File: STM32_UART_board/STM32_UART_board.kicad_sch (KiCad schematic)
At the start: 32 parts, among them J1 SWD, J2 Scooter, J3 Conn_01x10, Q1 AO4612_C4748739, SW1 SW_Push, SW2 SW_Push, U1 BAS70-05, U2 LM2574HVM-5, U3 AZ1117-3.3, U4 STM32C011F6Px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

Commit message: added testpoints to the remaining pins
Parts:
- added JP1, JP2, JP3: SolderJumper_3_Open, Jumper:SolderJumper-3_P1.3mm_Open_Pad1.0x1.5mm, symbol Jumper:SolderJumper_3_Open
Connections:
- net BOOT0_USART1_RX: now also JP2.3 (B)
- net BOOT0_USART1_TX: now also JP2.2 (C)
- net PA0: now also JP1.1 (A)
- net PA2: now also JP1.2 (C)
- net PA3: now also JP1.3 (B)
- net PA4: now also JP2.1 (A)
- net PB6: now also JP3.1 (A)
- net PB7: now also JP3.2 (C)
- net PC15: now also JP3.3 (B)

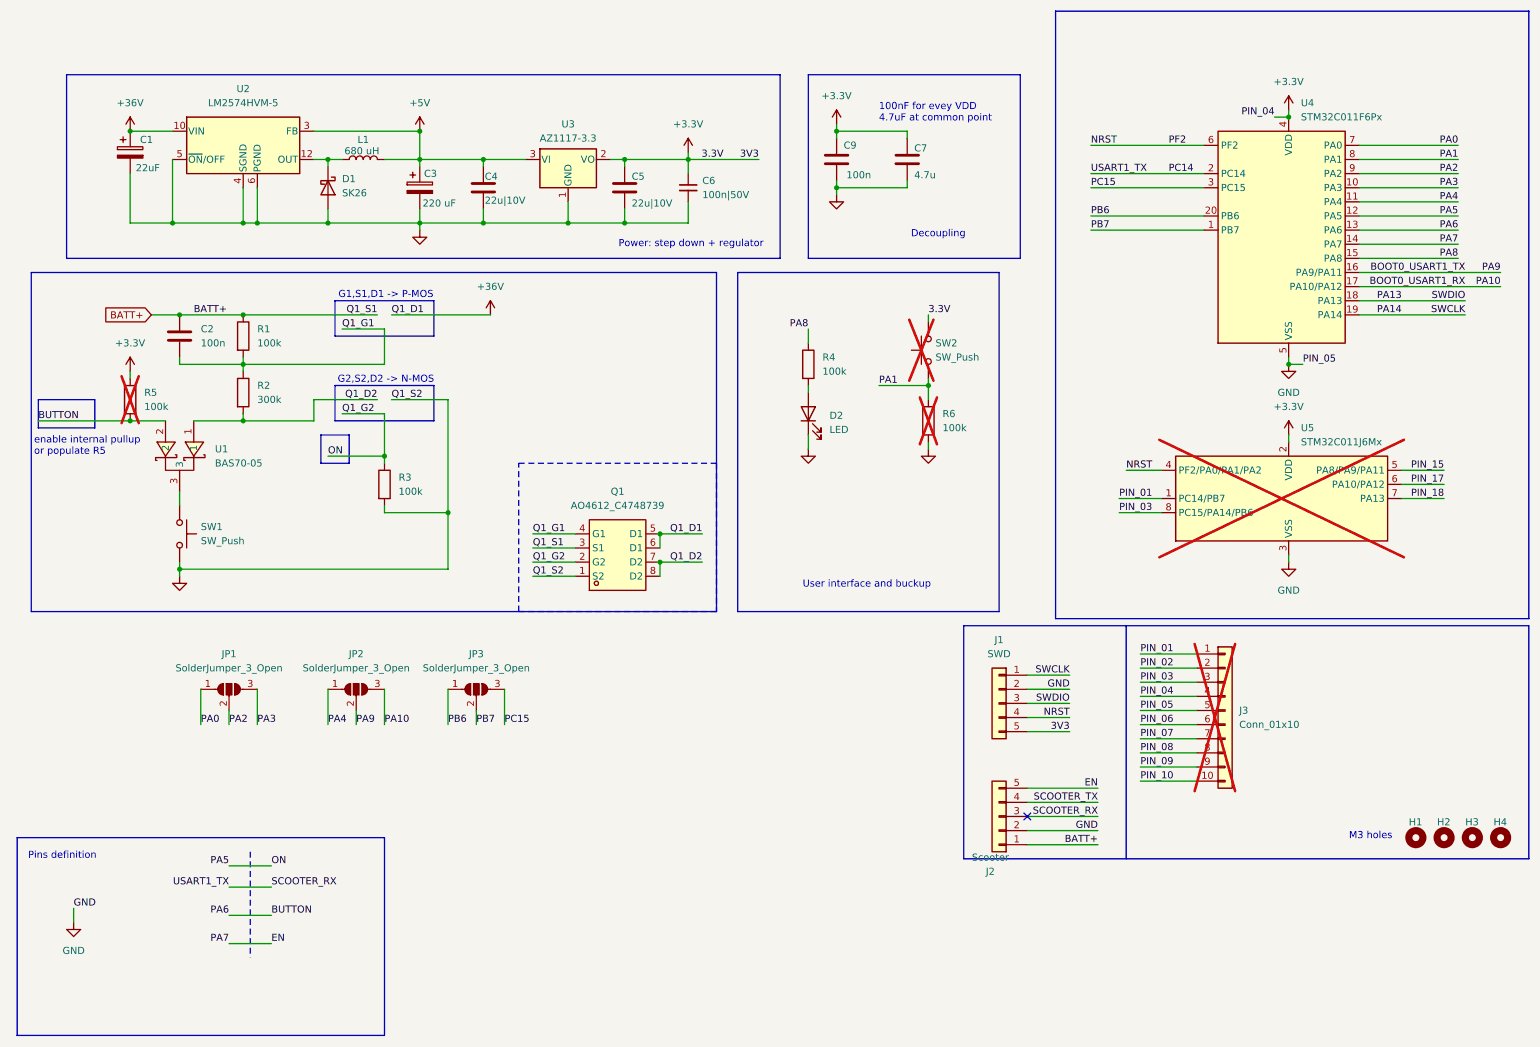
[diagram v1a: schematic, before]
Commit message: PCB with swapped RX TX | initial code fot STM32C011
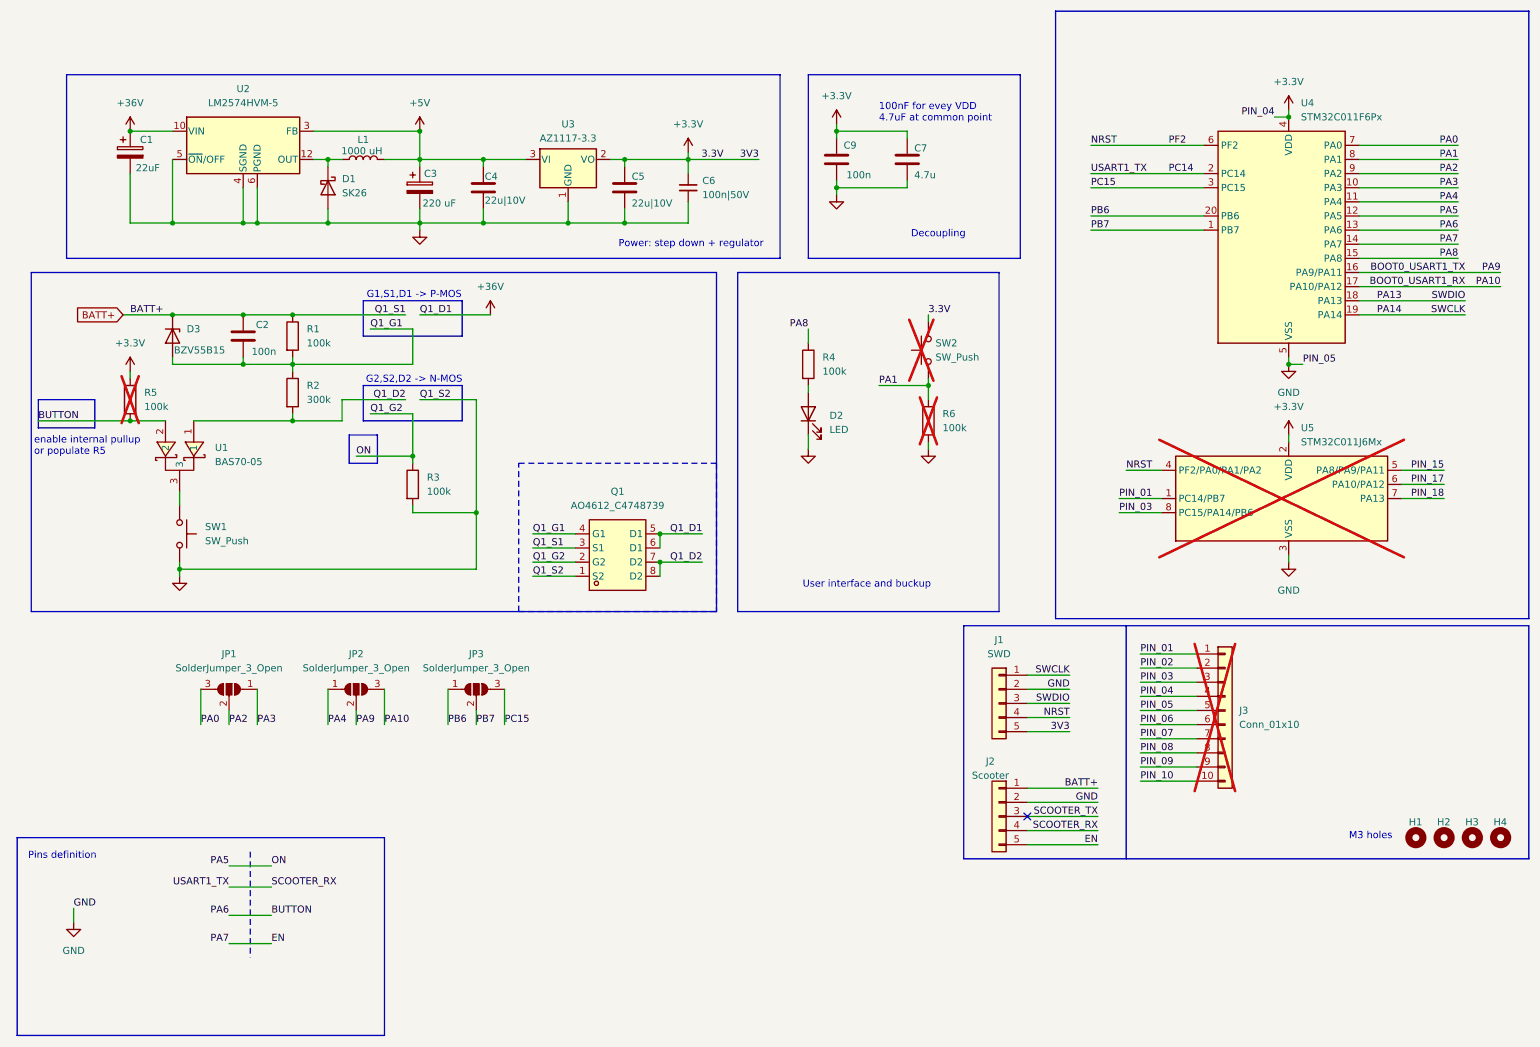
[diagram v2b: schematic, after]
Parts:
- added D3: BZV55B15, Diode_SMD:D_MiniMELF, symbol Diode:BZV55B15
- L1: value 680 uH -> 1000 uH
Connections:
- net BATT+: now also D3.1 (K)
- net PA0: now also JP1.3 (B); no longer JP1.1 (A)
- net PA3: now also JP1.1 (A); no longer JP1.3 (B)
- net PC14: now also J2.4 (Pin_4); no longer J2.3 (Pin_3)
- net Q1_G1: now also D3.2 (A)
- net SCOOTER_TX: now also J2.3 (Pin_3); no longer J2.4 (Pin_4)
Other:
- moved on the sheet: C2, J2, R1, R2, R3
